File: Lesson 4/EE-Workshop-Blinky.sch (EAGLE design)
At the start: 1 part

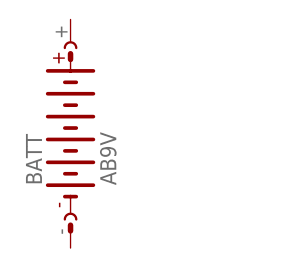
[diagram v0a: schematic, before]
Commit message: Updates to Workshop Lesson 4
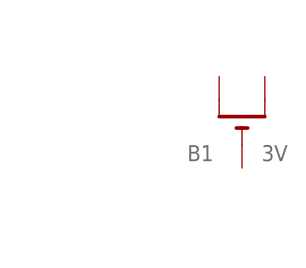
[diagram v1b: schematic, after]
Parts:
- removed BATT: AB9V, battery:AB9V
- added B1: 3V, adafruit:CR1220THM
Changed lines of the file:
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@@
 </classes>
 <parts>
-<part name="BATT" library="battery" library_urn="urn:adsk.eagle:library:109" deviceset="AB9V" device="" package3d_urn="urn:adsk.eagle:package:4600/1"/>
+<part name="B1" library="adafruit" library_urn="urn:adsk.eagle:library:420" deviceset="CR1220" device="THM" package3d_urn="urn:adsk.eagle:package:6240666/1" value="3V">
+<attribute name="SPICEPREFIX" value="J"/>
+</part>
 </parts>
 <sheets>
@@
 </plain>
 <instances>
-<instance part="BATT" gate="G$1" x="22.86" y="53.34" smashed="yes" rot="R90">
-<attribute name="NAME" x="19.685" y="47.625" size="1.778" layer="95" rot="R90"/>
-<attribute name="VALUE" x="27.94" y="47.625" size="1.778" layer="96" rot="R90"/>
+<instance part="B1" gate="G$1" x="41.91" y="54.61" smashed="yes" rot="R90">
+<attribute name="NAME" x="38.735" y="52.07" size="1.778" layer="95" rot="R180"/>
+<attribute name="VALUE" x="46.99" y="52.07" size="1.778" layer="96" rot="R180"/>
 </instance>
 </instances>
